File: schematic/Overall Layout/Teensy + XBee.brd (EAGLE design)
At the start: 60.9 x 60.6 mm, 13 parts, among them U4 MAX13054ASA

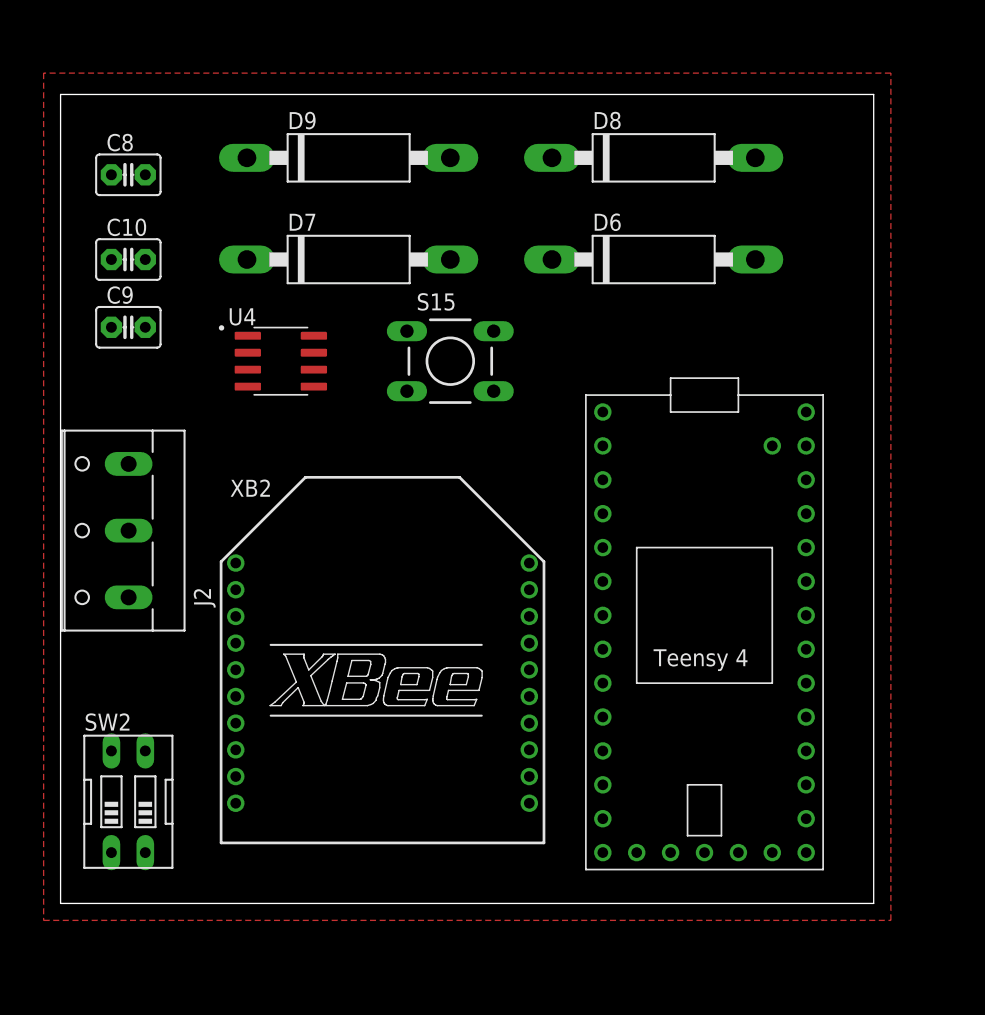
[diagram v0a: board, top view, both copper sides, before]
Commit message: Added military connectors to CAN Bus and added copper threading to PCB designs
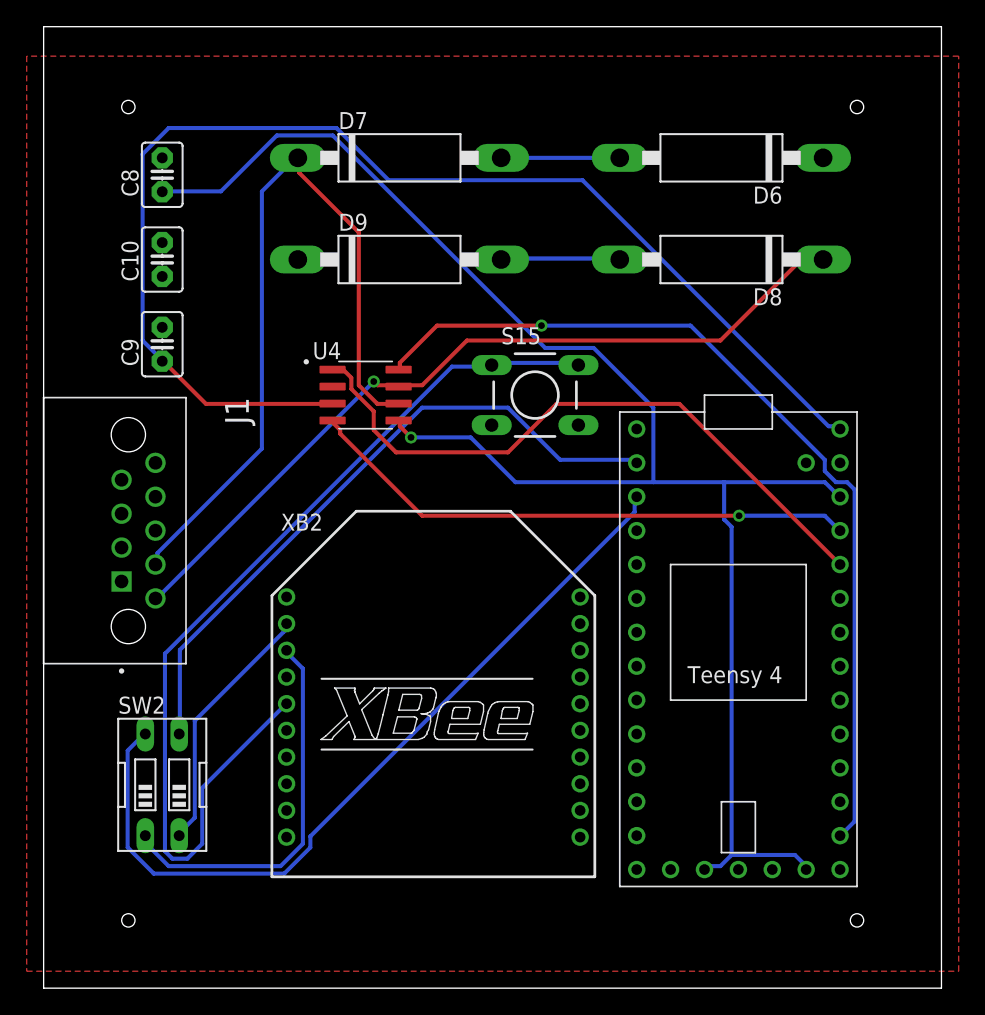
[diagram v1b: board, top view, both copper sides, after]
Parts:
- removed J2: (no value), con-wago-500:W237-103
- added J1: M83513/10-A01NP, M83513_10-A01NP:BEL_M83513/10-A01NP
- moved D6 9.16 mm to (49.5, 55.9), turned to 180 degrees
- moved D8 9.16 mm to (49.5, 48.3), turned to 180 degrees
- moved D7 8.52 mm to (25.4, 55.9)
- moved D9 8.52 mm to (25.4, 48.3)
- moved S15 6.84 mm to (35.6, 38.1)
- moved U4 6.84 mm to (22.9, 38.1)
- moved XB2 4.58 mm to (27.9, 14.0)
- moved C9 2.84 mm to (7.62, 41.9), turned to 90 degrees
- moved SW2 2.84 mm to (7.62, 8.89)
- moved U$6 2.84 mm to (50.8, 20.3)
- moved C10 2.54 mm to (7.62, 48.3), turned to 90 degrees
- moved C8 2.54 mm to (7.62, 54.6), turned to 90 degrees
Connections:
- net CAN_BUS: now also J1.6; no longer J2.1
- net GND: now also J1.8; no longer J2.3
- net N$3: now also J1.7; no longer J2.2
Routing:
- net +3V3: track 0.00 -> 125.2 mm, vias 0 -> 1
- net VCC: track 0.00 -> 92.7 mm
- net RESET: track 0.00 -> 71.5 mm
- net N$40: track 0.00 -> 67.7 mm, vias 0 -> 1
- net UART_TX: track 0.00 -> 60.9 mm
- net CAN_BUS: track 0.00 -> 60.9 mm, vias 0 -> 1
- net N$3: track 0.00 -> 57.6 mm
- net UART_RX: track 0.00 -> 49.8 mm
- net N$42: track 0.00 -> 48.4 mm
- net N$41: track 0.00 -> 41.7 mm, vias 0 -> 1
- net XBEE_IN: track 0.00 -> 28.8 mm
- net XBEE_OUT: track 0.00 -> 19.3 mm
- net N$45: track 0.00 -> 8.98 mm
- net N$44: track 0.00 -> 8.89 mm
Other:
- board size 60.9 x 60.6 mm -> 67.3 x 72.1 mm
